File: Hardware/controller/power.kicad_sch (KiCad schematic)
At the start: 18 parts, among them U201 BD9C301FJ

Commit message: Added Ethernet PHY
- Placed the Ethernet PHY on the controller board, and routed its lines
  to the rear panel connector. The MAC address will be stored in the NOR
  flash, and will need to be programmed in. (This avoids the complexity
  of needing a larger I2C switch to give us another bus for an I2C
  EEPROM; though we could ostensibly put one on the rear IO board.)
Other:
- title: (none) -> Power
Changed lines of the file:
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@@
 (kicad_sch (version 20211123) (generator eeschema)
   (paper "A4")
+  (title_block
+    (title "Power")
+    (date "2022-03-06")
+    (rev "1")
+  )
   (junction (at 95.25 26.035) (diameter 0) (color 0 0 0 0)
   )

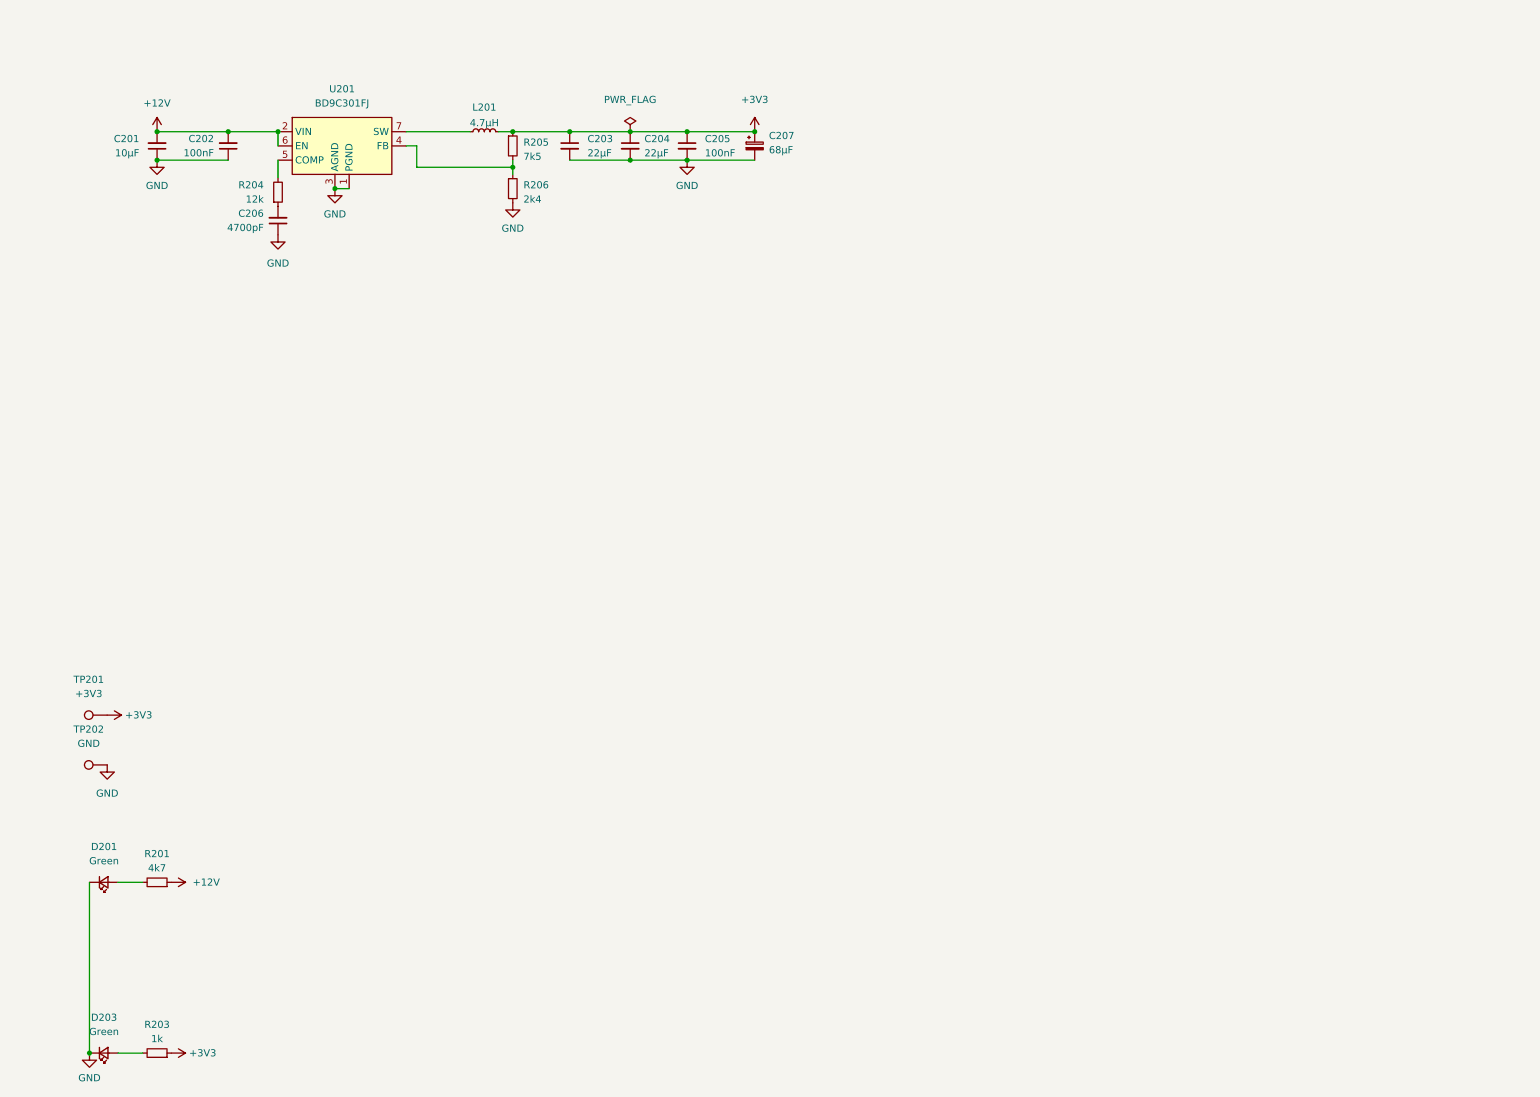
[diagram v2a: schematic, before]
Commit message: Re-design around STM32MP1 (#2)
* Start work on rev3 hardware

- This fits the Technomet R110 enclosure and supports multiple load
  boards, connected via CAN rather than I2C. Each load has a
  microcontroller of its own.

* More new layout stuff

- More work on the new controller board layout

- Rework rear IO board for the new Technomet rear panel (it has an
  expansion connector for CAN also, and features four screw holes
  instead of two)

- Added a few footprints (expansion RJ45 connector; some
  horizontal/vertical headers)

* Work on controller VSense, power

- Routed 3V3 switching supply

- Created footprint and symbols for Kemet EA2 series latching relay

- Added relays to controller to handle routing of voltage sense inputs
  to the sampling ADC

* Rear IO rework

- Mostly finished the rear IO board rework (adding the CAN filtering and
  switchable termination; trigger input pulse shaper; fuses for
  expansion +12V)

- Changed encoder type on front panel for a shorter type

- Created schematic models and footprints for Bournds DR311 chokes;
  Mill-Max 2108 solder turrets

* More work on new controller board

- Switched mains connection for a push-in screw terminal, rather than a
  pluggable block (takes up less space, less parts)

- Added input terminal for rear VSense inputs

- Added -5V supply (same circuit as on analog board; required for
  voltage input sense)

- Replaced beeper with a side-firing version. It takes up a bunch less
  space vertically, and also now added a resistor to (hopefully) make it
  somewhat more quiet

- Added connector for bonus displays

* Add "bonus display" board

- Created the bonus display board, which houses a chip-on-glass 4x10
  text character display. It's meant to be mounted next to the input
  jacks to show a constant location of current/voltage, even if the main
  display is used for menus or other stuff.

- More tweaks to controller board, to do with power g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
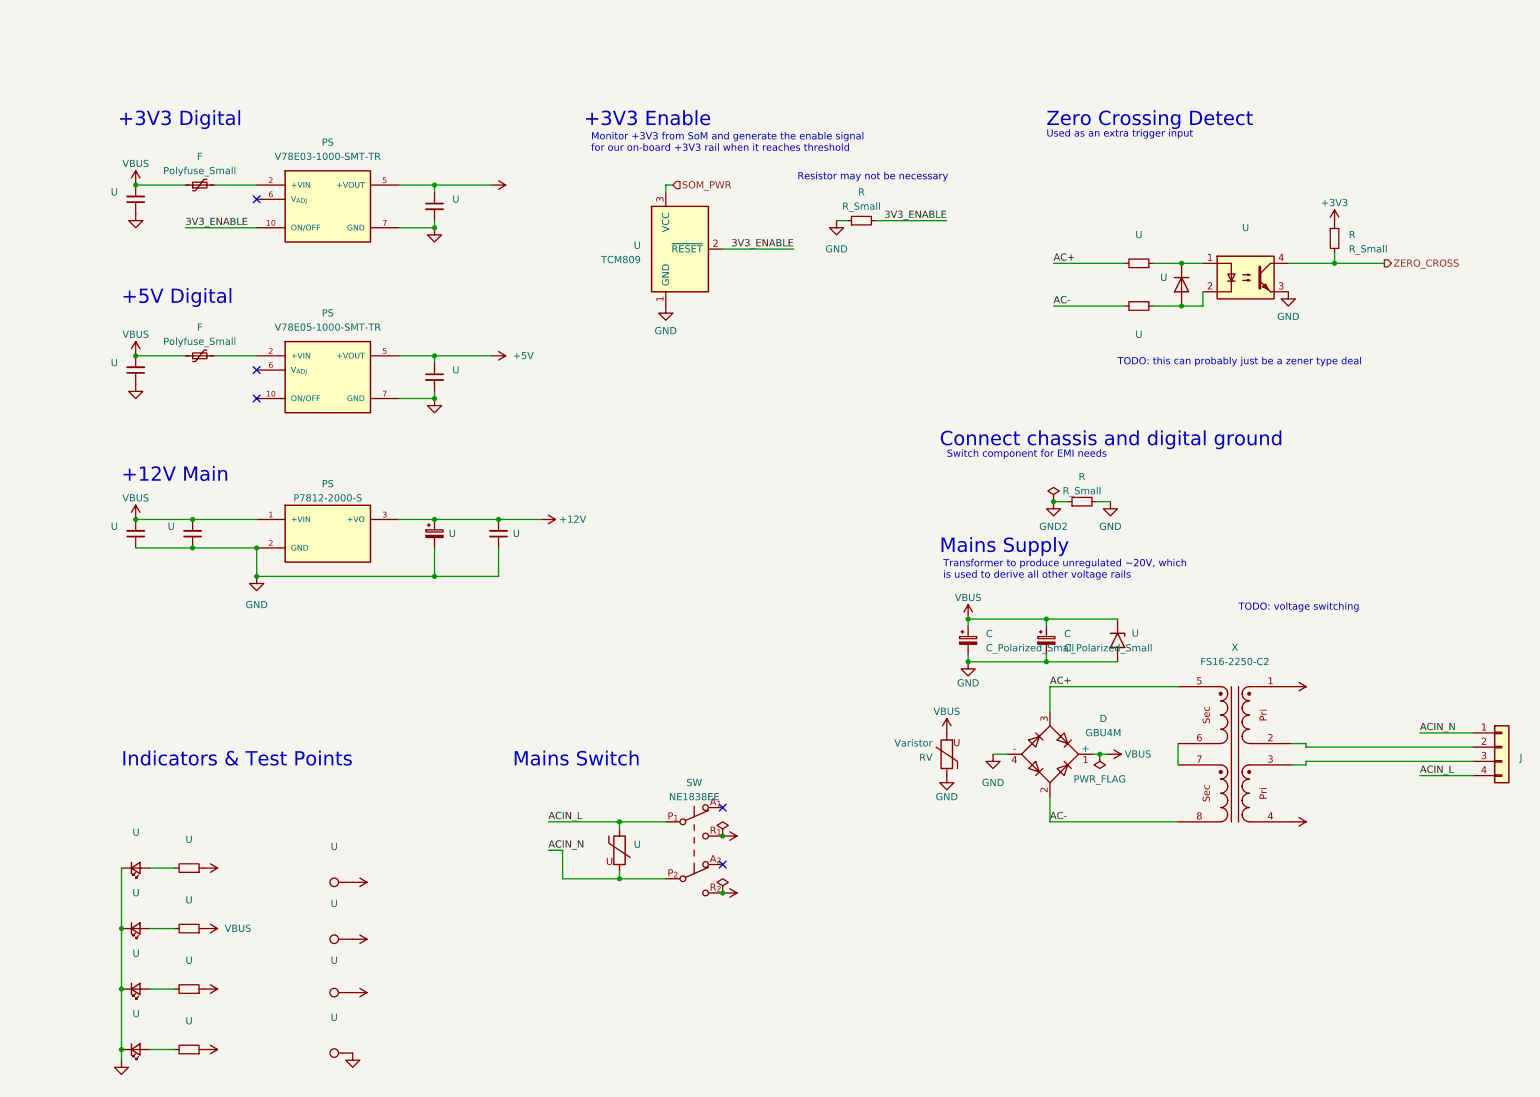
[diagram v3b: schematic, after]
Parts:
- removed C202, C205: 100nF, Capacitor_SMD:C_0805_2012Metric_Pad1.18x1.45mm_HandSolder, symbol Device:C_Small
- removed C204: 22µF, Capacitor_SMD:C_0805_2012Metric_Pad1.18x1.45mm_HandSolder, symbol Device:C_Small
- removed C206: 4700pF, Capacitor_SMD:C_0805_2012Metric_Pad1.18x1.45mm_HandSolder, symbol Device:C_Small
- removed C207: 68µF, Capacitor_THT:CP_Radial_D6.3mm_P2.50mm, symbol Device:C_Polarized_Small
- removed L201: 4.7µH, Inductor_SMD:L_Taiyo-Yuden_NR-80xx_HandSoldering, symbol Device:L_Small
- removed R204: 12k, Resistor_SMD:R_0805_2012Metric_Pad1.20x1.40mm_HandSolder, symbol Device:R_Small
- removed R205: 7k5, Resistor_SMD:R_0805_2012Metric_Pad1.20x1.40mm_HandSolder, symbol Device:R_Small
- removed R206: 2k4, Resistor_SMD:R_0805_2012Metric_Pad1.20x1.40mm_HandSolder, symbol Device:R_Small
- removed U201: BD9C301FJ, Package_SO:SOP-8_3.9x4.9mm_P1.27mm, symbol 68komputer-common:BD9C301FJ
- added C (x2): C_Polarized_Small, symbol Device:C_Polarized_Small
- added D: GBU4M, Diode_THT:Diode_Bridge_Vishay_GBU, symbol Diode_Bridge:GBU4M
- added F (x2): Polyfuse_Small, symbol Device:Polyfuse_Small
- added J: Conn_01x04, symbol Connector_Generic:Conn_01x04
- added PS: V78E03-1000-SMT-TR, programmable-load:CONV_V78E03-1000-SMT-TR, symbol programmable-load:V78E03-1000-SMT-TR
- added PS: V78E05-1000-SMT-TR, programmable-load:CONV_V78E03-1000-SMT-TR, symbol programmable-load:V78E05-1000-SMT-TR
- added PS: P7812-2000-S, programmable-load:CONV_P7812-2000-S, symbol programmable-load:P7812-2000-S
- added R (x3): R_Small, symbol Device:R_Small
- added RV: Varistor, symbol Device:Varistor
- added SW: NE1838EE, programmable-load:NE1838EE, symbol programmable-load:NE1838EE
- added U (x5): (no value), symbol Device:C_Small
- added U: (no value), symbol Diode:SM6T22A
- added U (x4): (no value), symbol Device:R_Small
- added U: TCM809, symbol Power_Supervisor:TCM809
- added U (x2): (no value), symbol Device:LED_Small
- added U (x2): (no value), symbol Connector:TestPoint
- added U: (no value), symbol Device:C_Polarized_Small
- added U: (no value), symbol Isolator:FODM217B
- added U: (no value), symbol Diode:1N4148W
- added U: (no value), symbol Device:Varistor
- added X: FS16-2250-C2, programmable-load:Triad-FS16-2250-C2, symbol programmable-load:FS20-1800-C2
- U: renamed from D203; value Green -> (none); footprint LED_SMD:LED_0805_2012Metric_Pad1.15x1.40mm_HandSolder -> (none)
- U: renamed from R203; value 1k -> (none); footprint Resistor_SMD:R_0805_2012Metric_Pad1.20x1.40mm_HandSolder -> (none); MPN CR0805-JW-102ELF -> (none)
- U: renamed from TP202; value GND -> (none); footprint TestPoint:TestPoint_Keystone_5000-5004_Miniature -> (none)
- U: renamed from C201; value 10µF -> (none); footprint Capacitor_SMD:C_0805_2012Metric_Pad1.18x1.45mm_HandSolder -> (none); MPN TMK212BBJ106KG-T -> GRM21BR61H106KE43K
- U: renamed from D201; value Green -> (none); footprint LED_SMD:LED_0805_2012Metric_Pad1.15x1.40mm_HandSolder -> (none)
- U: renamed from TP201; value +3V3 -> (none); footprint TestPoint:TestPoint_Keystone_5000-5004_Miniature -> (none)
- U: renamed from C203; value 22µF -> (none); footprint Capacitor_SMD:C_0805_2012Metric_Pad1.18x1.45mm_HandSolder -> (none)
- U: renamed from R201; value 4k7 -> (none); footprint Resistor_SMD:R_0805_2012Metric_Pad1.20x1.40mm_HandSolder -> (none); MPN 260-4.7K-RC -> (none)
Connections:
- net +12V: now also PS.3 (+VO), U.1, U.1, U.2; no longer U.2
- net +3V3: now also PS.4 (+VOUT), PS.5 (+VOUT), R.1
- net GND: now also C.2, C.2, D.4 (-), PS.2 (GND), PS.3 (GND), PS.3 (GND), PS.7 (GND), PS.7 (GND), R.1, R.2, RV.1, U.1, U.1, U.1, U.1, U.1 (GND), U.1 (K), U.1 (K), U.2, U.2, U.2 (A2), U.3
- new net: F.2, PS.1 (+VIN), PS.2 (+VIN) (x2)
- new net: U.2, U.2 (A) (x2)
- new net: U.1, U.1, U.1 (K)
- new net: J.2 (Pin_2), X.2
- new net: J.3 (Pin_3), X.3
- new net: X.6, X.7
- new net: U.1, U.2, U.2 (A)
- new net +5V: PS.4 (+VOUT), PS.5 (+VOUT), U.1, U.1, U.1
- new net 3V3_ENABLE: PS.10 (ON/OFF), R.2, U.2 (~{RESET})
- new net AC+: D.3, U.2, X.5
- new net AC-: D.2, U.2, X.8
- new net ACIN_L: J.4 (Pin_4), SW.P_{1} (B), U.1
- new net ACIN_N: J.1 (Pin_1), SW.P_{2} (B), U.2
- new net GND2: R.1
- new net LINE: SW.R_{1} (C), X.4
- new net NEUT: SW.R_{2} (C), X.1
- new net SOM_PWR: U.3 (VCC)
- new net VBUS: C.1, C.1, D.1 (+), F.1, F.1, PS.1 (+VIN), RV.2, U.1, U.1 (A1), U.2, U.2, U.2, U.2
- new net ZERO_CROSS: R.2, U.4
- no-connect marks 0 -> 5
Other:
- note added: "+12V Main"
- note added: "+3V3 Digital"
- note added: "+3V3 Enable"
- note added: "+5V Digital"
- note added: "Connect chassis and digital ground"
- note added: "Indicators & Test Points"
- note added: "Mains Supply"
- note added: "Mains Switch"
- note added: "Monitor +3V3 from SoM and generate the enable signal for our on-board +3V3 rail when it reaches threshold"
- note added: "Resistor may not be necessary"
- note added: "Switch component for EMI needs"
- note added: "TODO: this can probably just be a zener type deal"
- note added: "TODO: voltage switching"
- note added: "Transformer to produce unregulated ~20V, which is used to derive all other voltage rails"
- note added: "Used as an extra trigger input"
- note added: "Zero Crossing Detect"
- moved on the sheet: U

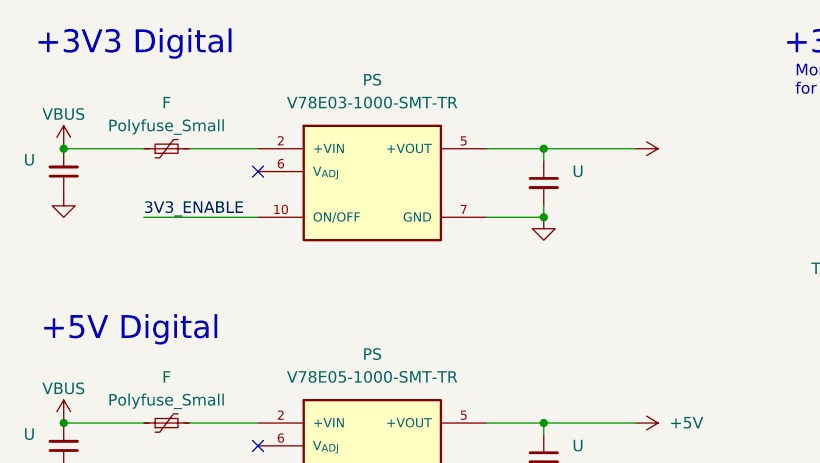
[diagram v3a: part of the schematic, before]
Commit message: hw: start working on rev4 controller
- removed SPI for display, and the associated SPI mux nonsense, and any
  superfluous resistors for pull-ups

- removed MAC address EEPROM

- start adding i2c RTC (which will also contain EEPROM with the MAC of
  the system, lol)

- start moving some components from bottom to top side of board

- tweaked positions of some mains voltage traces

- increased values of power indicator LED's current dropping resistors

- take 3V3 from SoM rather than generate it ourselves
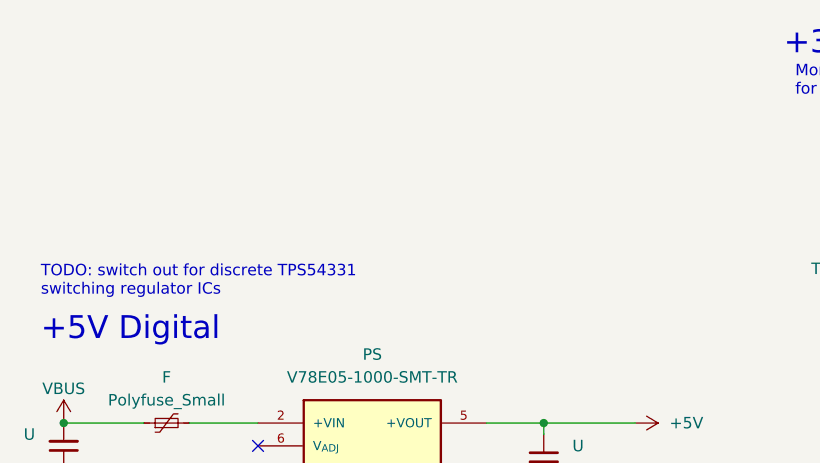
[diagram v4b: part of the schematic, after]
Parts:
- removed F: Polyfuse_Small, symbol Device:Polyfuse_Small
- removed PS: V78E03-1000-SMT-TR, programmable-load:CONV_V78E03-1000-SMT-TR, symbol programmable-load:V78E03-1000-SMT-TR
- removed U (x2): (no value), symbol Device:C_Small
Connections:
- no-connect marks 5 -> 4
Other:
- note added: "TODO: switch out for discrete TPS54331 switching regulator ICs"
- note removed: "+3V3 Digital"
- title: Power -> Programmable Load Controller
